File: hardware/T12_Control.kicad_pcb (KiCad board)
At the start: 2 copper layers, 49.5 x 38.2 mm, 39 parts, among them J1 Screw_Terminal_01x02, J2 GX12-5M, J3 SPI LCD, J4 I2C LCD, J5 SWD, J6 Serial, Q1 TPC8107, Q2 SI2308A, U1 AMS1117-3.3, U2 24LC32, U3 SGM8551XN, U4 STM32F103CBTx

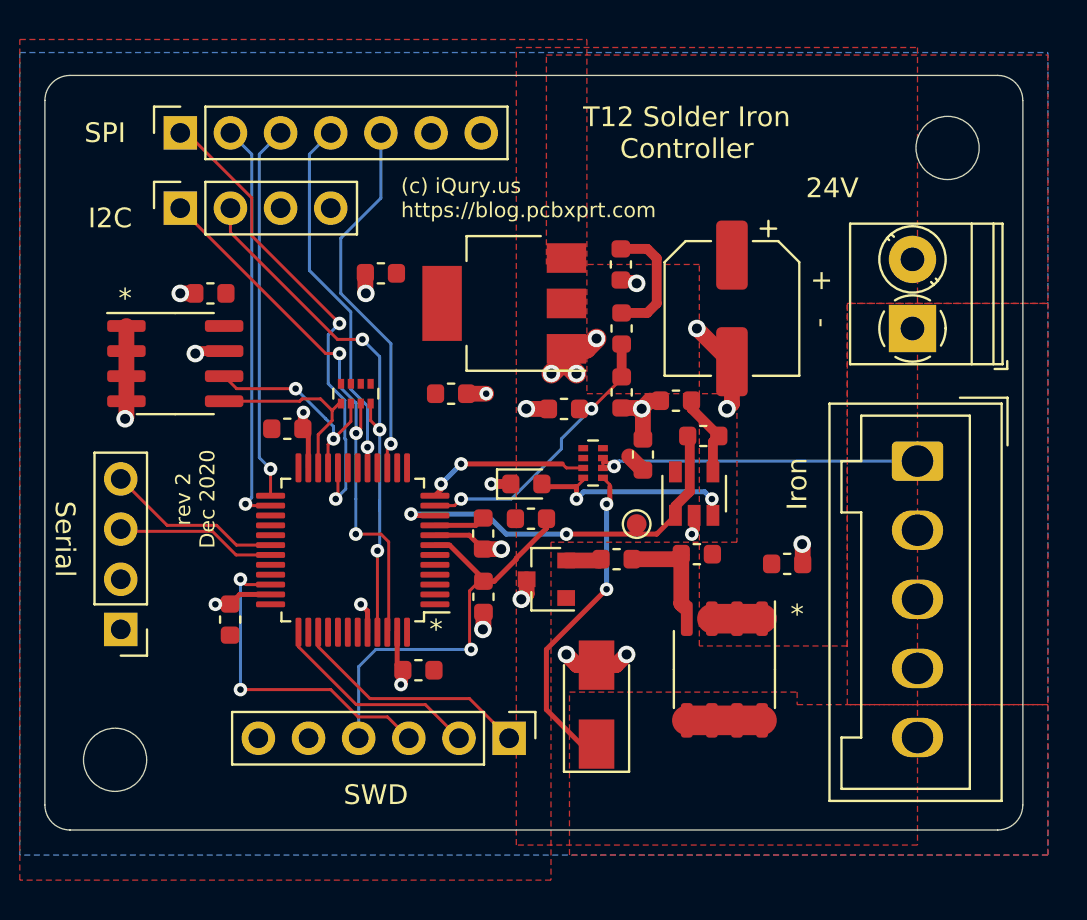
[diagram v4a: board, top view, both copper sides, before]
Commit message: Rotate the display connectors 180 degrees. Add extra filter cap on pin 1 (VBAT). Improve PCB layout.
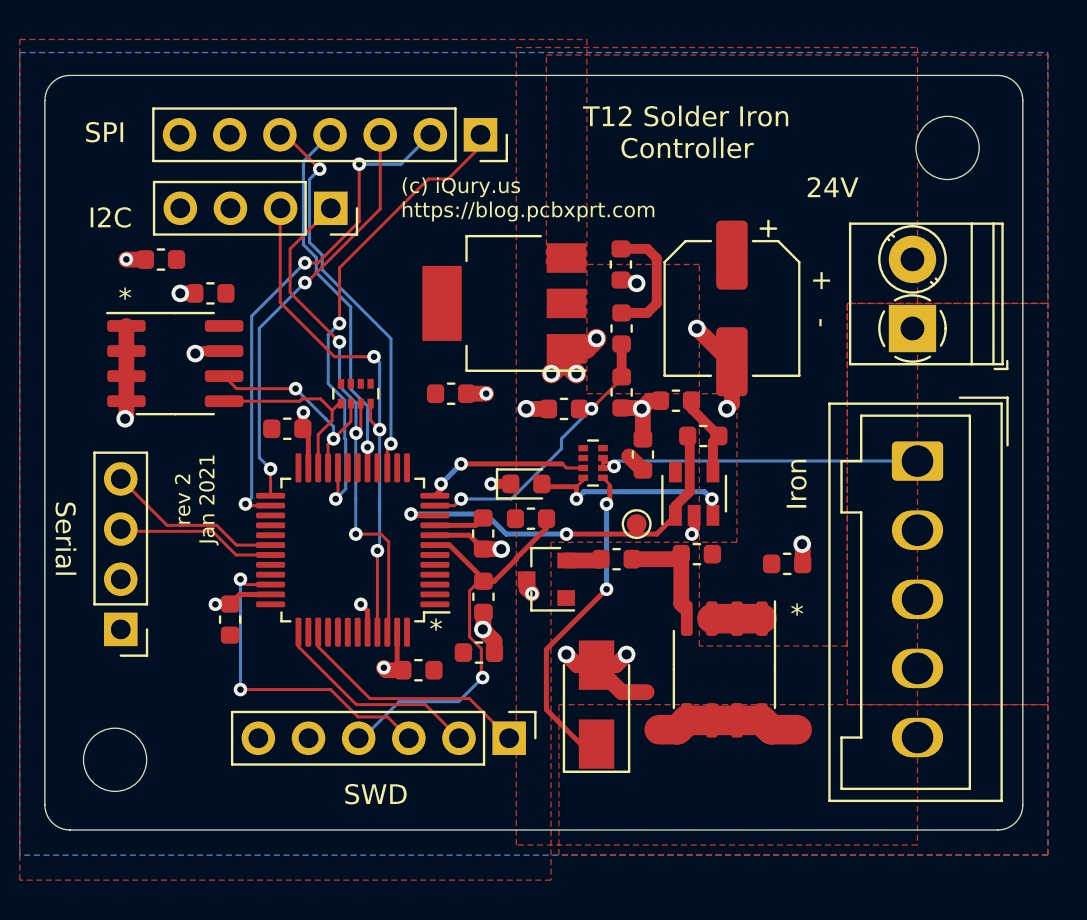
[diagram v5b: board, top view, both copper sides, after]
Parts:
- added C14: 100nF, Capacitor_SMD:C_0603_1608Metric, F.Cu at (217.6, 100.2)
- moved J3 15.2 mm to (217.6, 74.0), turned to -90 degrees
- moved C5 11.2 mm to (201.5, 80.3)
- moved J4 7.62 mm to (210.1, 77.7), turned to -90 degrees
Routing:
- net /D/~C: track 20.7 -> 25.6 mm, vias 1 -> 3
- net GND: track 47.0 -> 51.5 mm
- net Net-(D1-Pad1): track 20.3 -> 23.9 mm
- net /~RST: track 19.1 -> 21.1 mm, vias 1 -> 2
- net /OLED_SDA: track 28.6 -> 26.8 mm
- net /SCK: track 18.9 -> 19.9 mm, vias 1 -> 2
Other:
- board text added: "rev 2 Jan 2021"
- board text removed: "rev 2 Dec 2020"

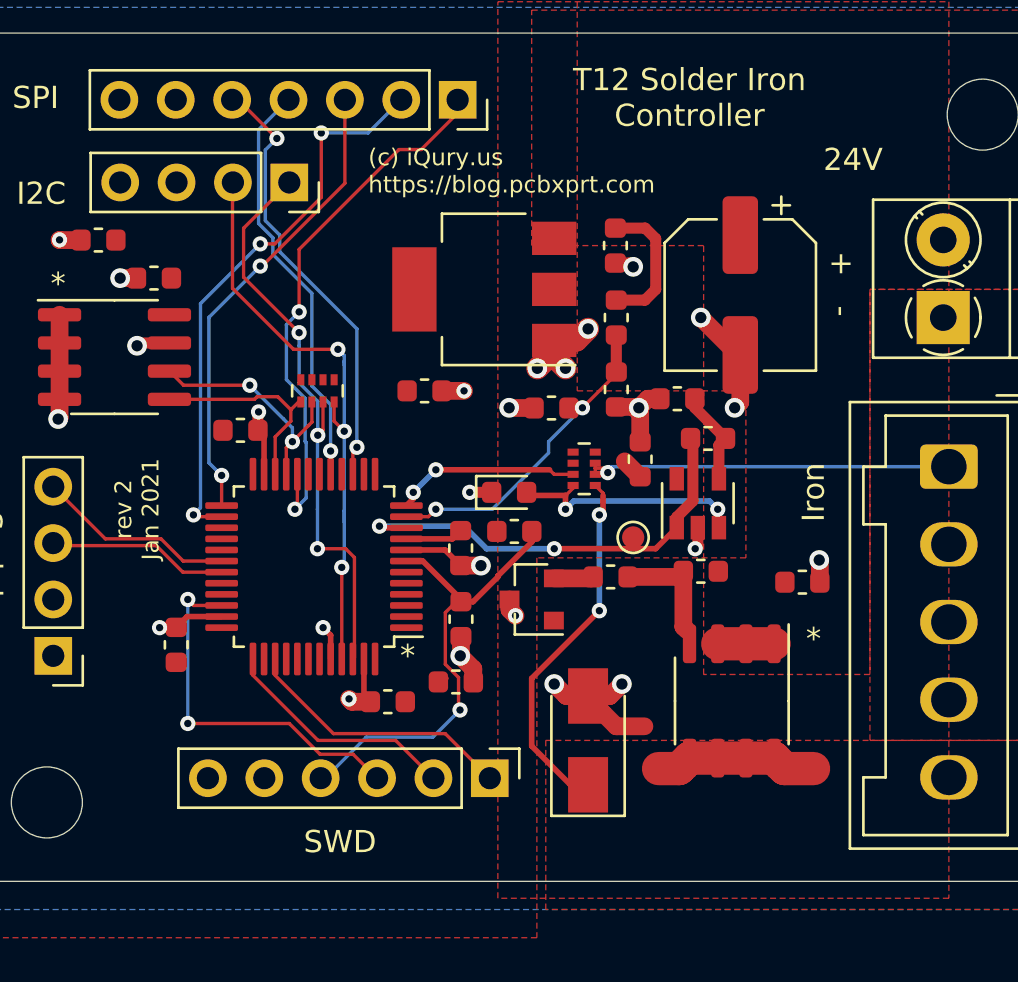
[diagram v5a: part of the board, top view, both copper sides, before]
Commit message: Updated soldering iron board.
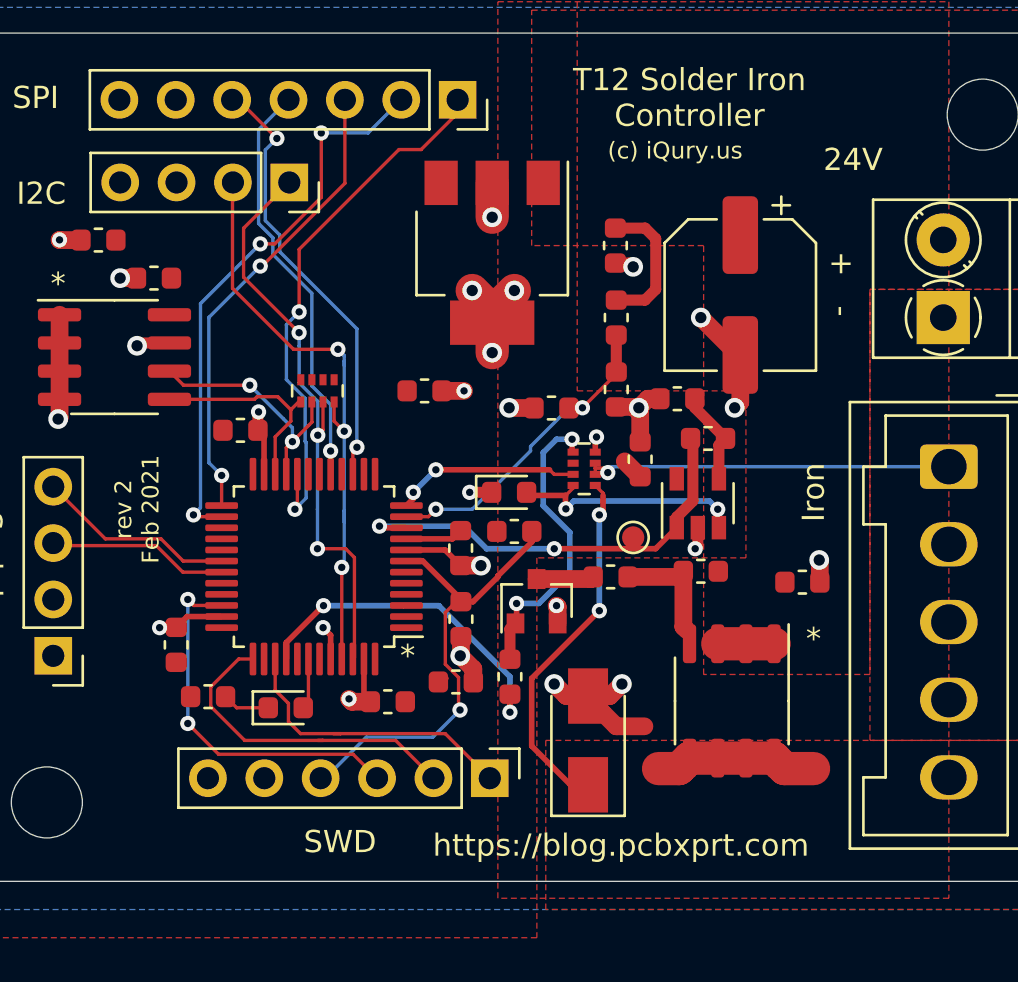
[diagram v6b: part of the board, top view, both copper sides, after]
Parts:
- added D3: RED, LED_SMD:LED_0603_1608Metric, F.Cu at (209.9, 101.4)
- added R8: 470, Resistor_SMD:R_0603_1608Metric, F.Cu at (220.0, 100.0)
- added R9: 1k, Resistor_SMD:R_0603_1608Metric, F.Cu at (206.4, 100.9)
- Q2: value SI2308A -> BC817
- U1: value AMS1117-3.3 -> SPX2954M3-3.3_SOT223
- moved U1 1.69 mm to (219.2, 80.9), turned to -90 degrees
- moved Q2 0.23 mm to (221.2, 96.6), turned to 90 degrees
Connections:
- Q2 pad 1: (no net) -> Net-(Q2-Pad1)
- Q2 pad 2: Net-(Q2-Pad2) -> GND
- Q2 pad 3: GND -> Net-(Q2-Pad3)
- R3 pad 2: Net-(Q2-Pad2) -> Net-(Q2-Pad3)
- RN1 pad 1: (no net) -> Net-(Q2-Pad1)
- RN1 pad 8: (no net) -> GND
- U1 pad 1: GND -> /24V
- U1 pad 2: /3.3V -> GND
- U1 pad 3: /24V -> /3.3V
- U4 pad 40: (no net) -> /HEATER_ON
- U4 pad 42: (no net) -> Net-(D3-Pad2)
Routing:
- net /HEATER_ON: track 0.00 -> 15.2 mm, vias 0 -> 2
- net Net-(Q2-Pad1): track 0.00 -> 13.7 mm, vias 0 -> 2
- net /SWDCLK: track 10.8 -> 14.9 mm
- net Net-(Q2-Pad3): track 0.00 -> 2.68 mm
- net GND: track 51.5 -> 54.0 mm, vias 25 -> 27
- net Net-(D3-Pad2): track 0.00 -> 2.29 mm
- net Net-(D3-Pad1): track 0.00 -> 2.13 mm
- net Net-(Q2-Pad2): track 1.80 -> 0.00 mm
- net /SWDSWO: track 12.3 -> 13.5 mm
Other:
- board text added: "(c) iQury.us"
- board text added: "https://blog.pcbxprt.com"
- board text added: "rev 2 Feb 2021"
- board text removed: "(c) iQury.us https://blog.pcbxprt.com"
- board text removed: "rev 2 Jan 2021"

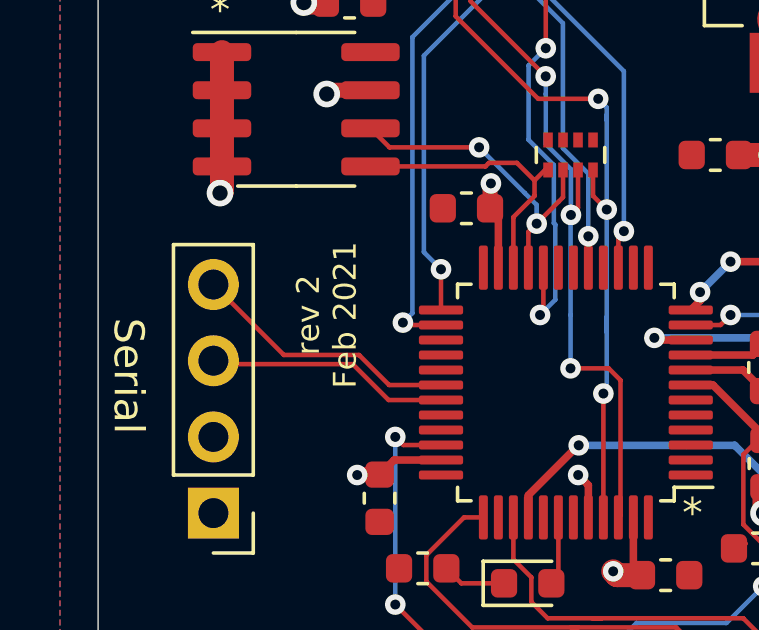
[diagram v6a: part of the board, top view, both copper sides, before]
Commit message: Start Soldering Iron r3.
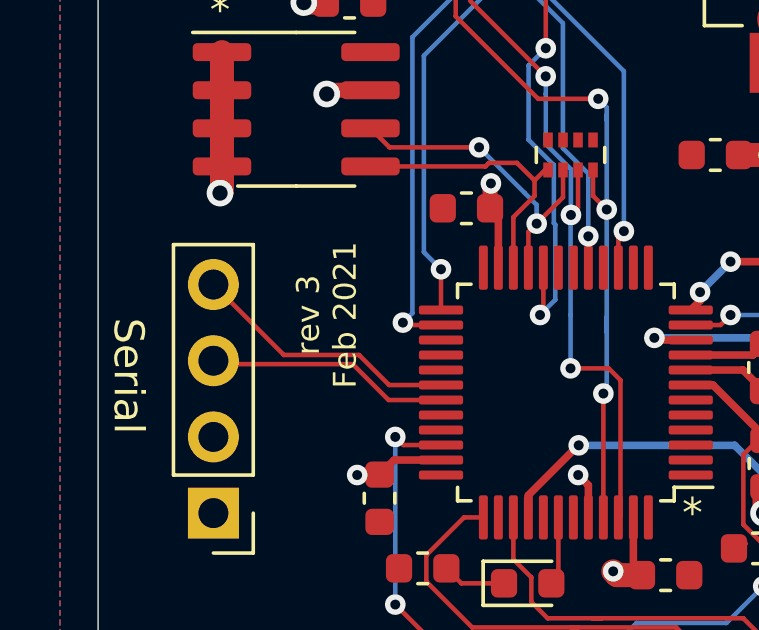
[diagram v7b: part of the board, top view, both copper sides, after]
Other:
- board text added: "rev 3 Feb 2021"
- board text removed: "rev 2 Feb 2021"
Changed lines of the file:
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@@
     (effects (font (size 1 1) (thickness 0.15)) (justify mirror))
   )
-  (gr_text "rev 2\nFeb 2021" (at 203.2 92.456 90) (layer "F.SilkS")
+  (gr_text "rev 3\nFeb 2021" (at 203.2 92.456 90) (layer "F.SilkS")
     (effects (font (size 0.762 0.762) (thickness 0.1016)))
   )

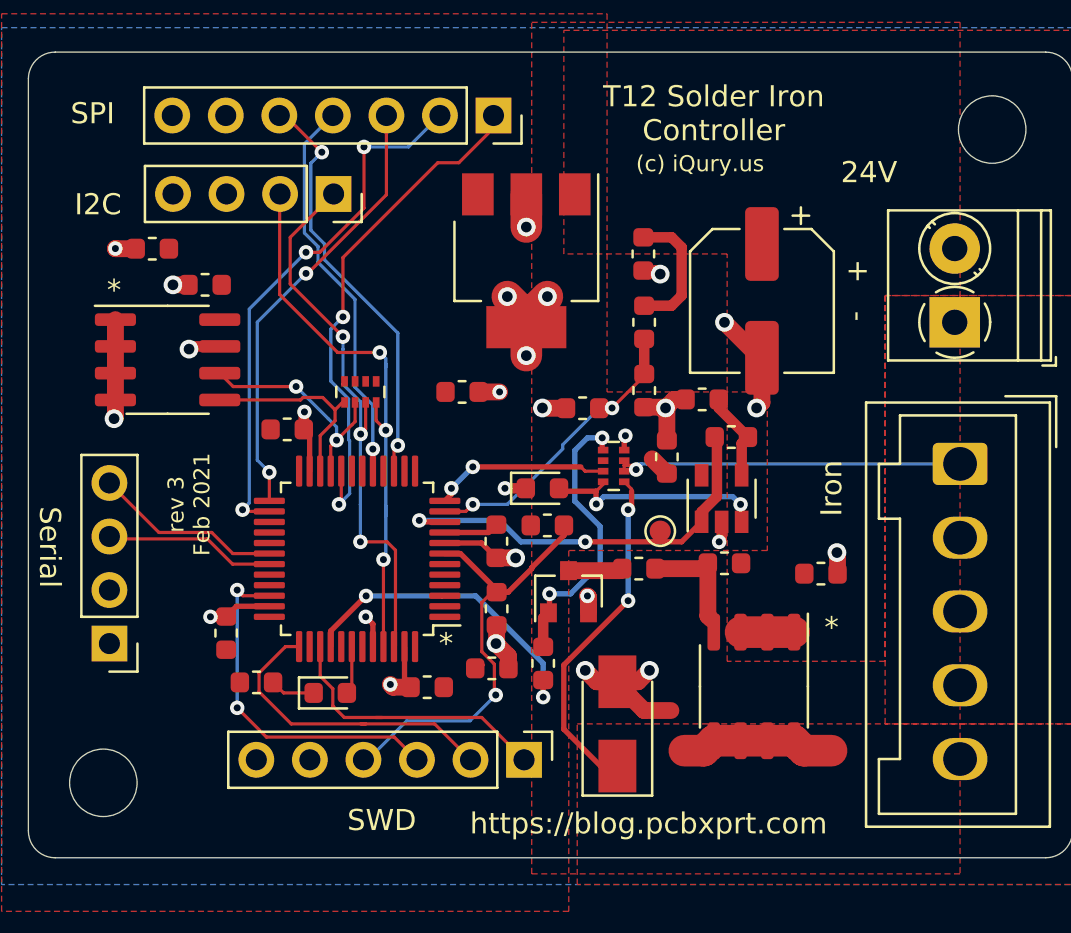
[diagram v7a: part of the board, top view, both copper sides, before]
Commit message: Improve power supply filtering.
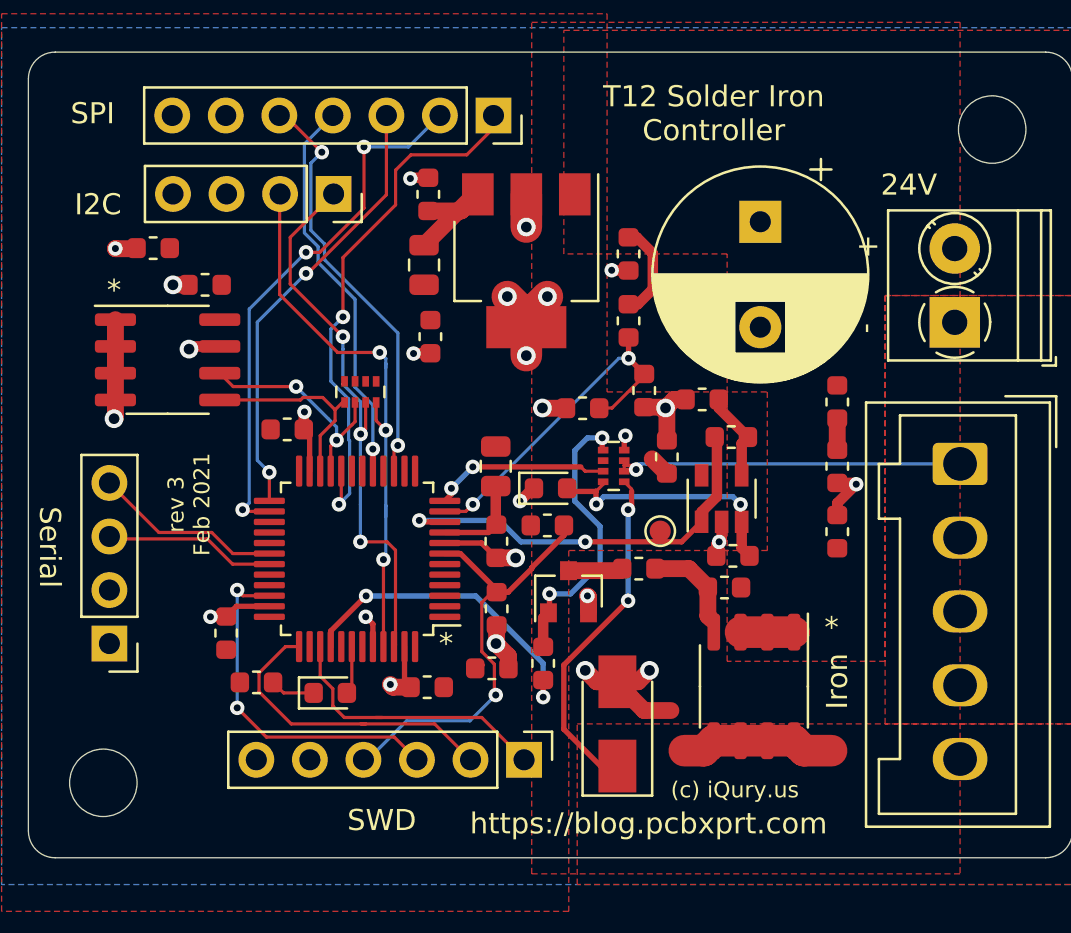
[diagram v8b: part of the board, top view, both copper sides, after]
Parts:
- added C15: 1nF, Capacitor_SMD:C_0603_1608Metric, F.Cu at (229.0, 94.9)
- added C16: 470pF, Capacitor_SMD:C_0603_1608Metric, F.Cu at (233.9, 90.7)
- added C17: 100nF, Capacitor_SMD:C_0603_1608Metric, F.Cu at (201.5, 80.3)
- added FB1: Ferrite_Bead, Inductor_SMD:L_0805_2012Metric, F.Cu at (214.3, 81.1)
- added FB2: Ferrite_Bead, Inductor_SMD:L_0805_2012Metric, F.Cu at (217.8, 90.7)
- added R10: 2.2, Resistor_SMD:R_0603_1608Metric, F.Cu at (233.9, 87.6)
- C12: footprint Capacitor_SMD:CP_Elec_6.3x7.7 -> Capacitor_THT:CP_Radial_D10.0mm_P5.00mm
- moved C5 13.3 mm to (214.6, 77.8), turned to 90 degrees
- moved C12 3.75 mm to (230.3, 79.0)
- moved C3 3.02 mm to (214.7, 84.5), turned to -90 degrees
- moved C1 2.14 mm to (233.9, 93.8), turned to 90 degrees
- moved R1 1.15 mm to (228.6, 96.4)
- moved R2 0.74 mm to (224.1, 83.8)
- moved C2 0.70 mm to (224.1, 80.6)
- moved D2 0.39 mm to (220.3, 91.7)
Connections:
- C10 pad 1: /3.3V -> Net-(C10-Pad1)
- C5 pad 1: /3.3V -> Net-(C5-Pad1)
- U1 pad 3: /3.3V -> Net-(C5-Pad1)
- U4 pad 9: /3.3V -> Net-(C10-Pad1)
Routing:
- net Net-(C5-Pad1): track 0.00 -> 6.23 mm
- net Net-(C10-Pad1): track 0.00 -> 4.44 mm
- net /3.3V: track 3.70 -> 1.10 mm
- net /V_MON: track 14.6 -> 16.6 mm
- net GND: track 54.0 -> 52.0 mm, vias 27 -> 26
- net /24V: track 8.82 -> 7.15 mm
- net Net-(C16-Pad1): track 0.00 -> 1.47 mm
- net Net-(C15-Pad1): track 11.0 -> 12.4 mm
- net /~CS: track 24.4 -> 25.4 mm
- net Net-(Q1-Pad4): track 5.31 -> 4.42 mm
